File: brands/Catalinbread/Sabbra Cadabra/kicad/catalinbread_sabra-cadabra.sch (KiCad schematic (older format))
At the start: 62 parts

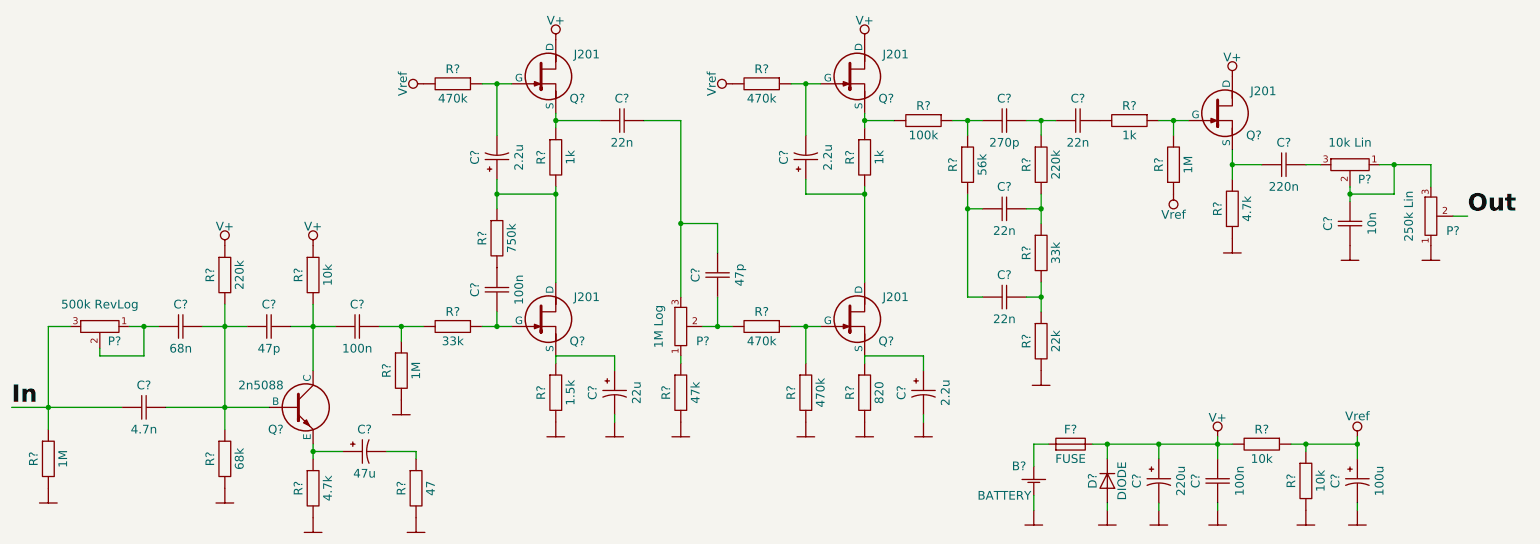
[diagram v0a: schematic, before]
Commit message: Catalinbread Sabra Cadabra. Fixed KiCAD schematic, added png chematic, added slayout
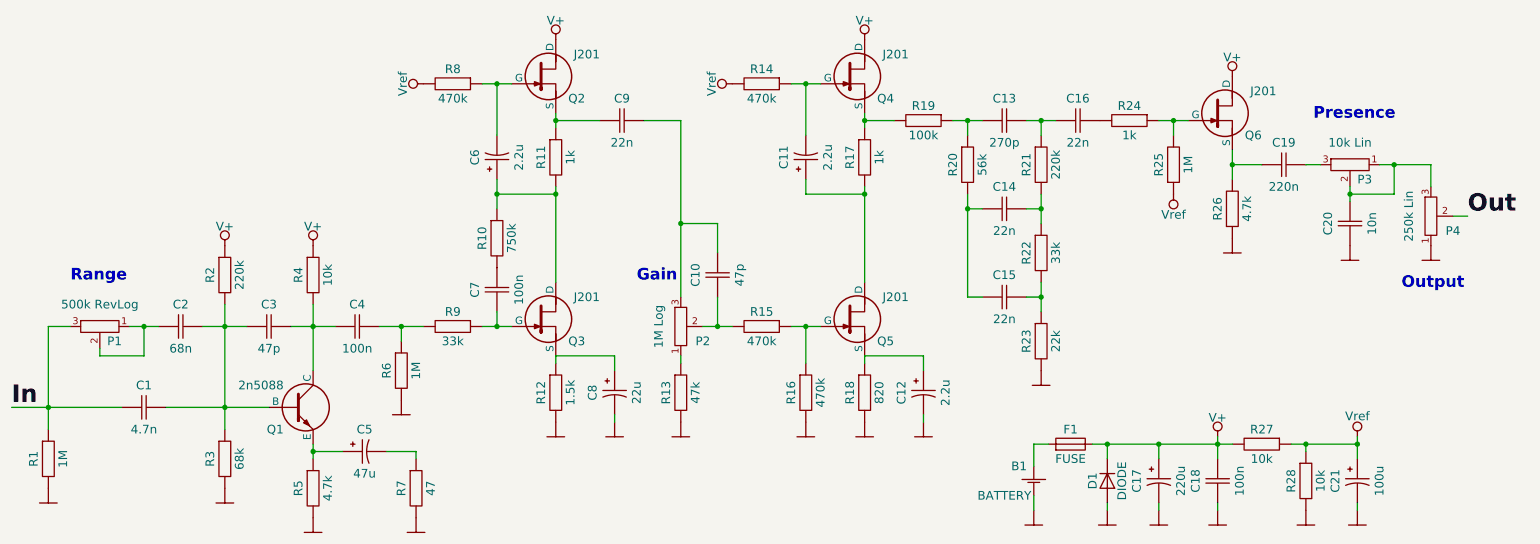
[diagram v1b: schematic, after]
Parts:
- gave numbers to parts that had none: 62
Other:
- note added: "Gain"
- note added: "Output"
- note added: "Presence"
- note added: "Range"
